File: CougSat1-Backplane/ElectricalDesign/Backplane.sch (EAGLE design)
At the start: 20 parts, among them J1 CougSat Socket, J10 CougSat Socket, J2 CougSat Socket, J3 CougSat Socket, J4 CougSat Socket, J5 Separation Switch, J6 Separation Switch, J7 CougSat Socket, J8 CougSat Socket, J9 CougSat Socket

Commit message: Removed Unused Connectors, Shrunk Outline
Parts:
- removed J1, J2, J3: CougSat Socket, CougsInSpace-Connectors:CIS_CARD-PCIE
- removed J5, J6: Separation Switch, CougsInSpace-Connectors:1X04-PICOLOCK
- removed LOGO1: Text, CougsInSpace-Aesthetics:CIS-LOGO-TEXT
- removed LOGO100, LOGO3: Satellite 16mm, CougsInSpace-Aesthetics:CIS-LOGO-SATELLITE-16MM
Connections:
- net BUS_I2C0_IRQ: no longer J1DATA.BUS_I2C0_IRQ, J2DATA.BUS_I2C0_IRQ, J3DATA.BUS_I2C0_IRQ
- net BUS_I2C0_SCL: no longer J1DATA.BUS_I2C0_SCL, J2DATA.BUS_I2C0_SCL, J3DATA.BUS_I2C0_SCL
- net BUS_I2C0_SDA: no longer J1DATA.BUS_I2C0_SDA, J2DATA.BUS_I2C0_SDA, J3DATA.BUS_I2C0_SDA
- net BUS_I2C1_IRQ: no longer J1DATA.BUS_I2C1_IRQ, J2DATA.BUS_I2C1_IRQ, J3DATA.BUS_I2C1_IRQ
- net BUS_I2C1_SCL: no longer J1DATA.BUS_I2C1_SCL, J2DATA.BUS_I2C1_SCL, J3DATA.BUS_I2C1_SCL
- net BUS_I2C1_SDA: no longer J1DATA.BUS_I2C1_SDA, J2DATA.BUS_I2C1_SDA, J3DATA.BUS_I2C1_SDA
- net BUS_JTAG_EN-0: no longer J1JTAG.BUS_JTAG_EN-0, J2JTAG.BUS_JTAG_EN-0, J3JTAG.BUS_JTAG_EN-0
- net BUS_JTAG_EN-1: no longer J1JTAG.BUS_JTAG_EN-1, J2JTAG.BUS_JTAG_EN-1, J3JTAG.BUS_JTAG_EN-1
- net BUS_JTAG_EN-2: no longer J1JTAG.BUS_JTAG_EN-2, J2JTAG.BUS_JTAG_EN-2, J3JTAG.BUS_JTAG_EN-2
- net BUS_JTAG_EN-3: no longer J1JTAG.BUS_JTAG_EN-3, J2JTAG.BUS_JTAG_EN-3, J3JTAG.BUS_JTAG_EN-3
- net BUS_JTAG_TCK: no longer J1JTAG.BUS_JTAG_TCK, J2JTAG.BUS_JTAG_TCK, J3JTAG.BUS_JTAG_TCK
- net BUS_JTAG_TDI: no longer J1JTAG.BUS_JTAG_TDI, J2JTAG.BUS_JTAG_TDI, J3JTAG.BUS_JTAG_TDI
- net BUS_JTAG_TDO: no longer J1JTAG.BUS_JTAG_TDO, J2JTAG.BUS_JTAG_TDO, J3JTAG.BUS_JTAG_TDO
- net BUS_JTAG_TMS: no longer J1JTAG.BUS_JTAG_TMS, J2JTAG.BUS_JTAG_TMS, J3JTAG.BUS_JTAG_TMS
- net BUS_SPI_MISO: no longer J1DATA.BUS_SPI_MISO, J2DATA.BUS_SPI_MISO, J3DATA.BUS_SPI_MISO
- net BUS_SPI_MOSI: no longer J1DATA.BUS_SPI_MOSI, J2DATA.BUS_SPI_MOSI, J3DATA.BUS_SPI_MOSI
- net BUS_SPI_SCK: no longer J1DATA.BUS_SPI_SCK, J2DATA.BUS_SPI_SCK, J3DATA.BUS_SPI_SCK
- net COM_SPI_CS: no longer J1DATA.COM_SPI_CS, J2DATA.COM_SPI_CS, J3DATA.COM_SPI_CS
- net COM_SPI_MISO: no longer J1DATA.COM_SPI_MISO, J2DATA.COM_SPI_MISO, J3DATA.COM_SPI_MISO
- net COM_SPI_MOSI: no longer J1DATA.COM_SPI_MOSI, J2DATA.COM_SPI_MOSI, J3DATA.COM_SPI_MOSI
- net COM_SPI_SCK: no longer J1DATA.COM_SPI_SCK, J2DATA.COM_SPI_SCK, J3DATA.COM_SPI_SCK
- net CTRL_SYNC: no longer J1DATA.CTRL_SYNC, J2DATA.CTRL_SYNC, J3DATA.CTRL_SYNC
- net GPIO-0: no longer J1GPIO.GPIO-0, J2GPIO.GPIO-0, J3GPIO.GPIO-0
- net GPIO-1: no longer J1GPIO.GPIO-1, J2GPIO.GPIO-1, J3GPIO.GPIO-1
- net GPIO-2: no longer J1GPIO.GPIO-2, J2GPIO.GPIO-2, J3GPIO.GPIO-2
- net GPIO-3: no longer J1GPIO.GPIO-3, J2GPIO.GPIO-3, J3GPIO.GPIO-3
- net GPIO-4: no longer J1GPIO.GPIO-4, J2GPIO.GPIO-4, J3GPIO.GPIO-4
- net GPIO-5: no longer J1GPIO.GPIO-5, J2GPIO.GPIO-5, J3GPIO.GPIO-5
- net GPIO-6: no longer J1GPIO.GPIO-6, J2GPIO.GPIO-6, J3GPIO.GPIO-6
- net GPIO-7: no longer J1GPIO.GPIO-7, J2GPIO.GPIO-7, J3GPIO.GPIO-7
- net PGND: no longer J1POWER.PGND, J2POWER.PGND, J3POWER.PGND, J5.3, J5.4, J6.3, J6.4
- net PR_3.3V-0: no longer J1POWER.PR_3.3V-0, J2POWER.PR_3.3V-0, J3POWER.PR_3.3V-0
- net PR_3.3V-1: no longer J1POWER.PR_3.3V-1, J2POWER.PR_3.3V-1, J3POWER.PR_3.3V-1
- net PR_3.3V-10: no longer J1POWER.PR_3.3V-10, J2POWER.PR_3.3V-10, J3POWER.PR_3.3V-10
- net PR_3.3V-11: no longer J1POWER.PR_3.3V-11, J2POWER.PR_3.3V-11, J3POWER.PR_3.3V-11
- net PR_3.3V-12: no longer J1POWER.PR_3.3V-12, J2POWER.PR_3.3V-12, J3POWER.PR_3.3V-12
- net PR_3.3V-2: no longer J1POWER.PR_3.3V-2, J2POWER.PR_3.3V-2, J3POWER.PR_3.3V-2
- net PR_3.3V-3: no longer J1POWER.PR_3.3V-3, J2POWER.PR_3.3V-3, J3POWER.PR_3.3V-3
- net PR_3.3V-4: no longer J1POWER.PR_3.3V-4, J2POWER.PR_3.3V-4, J3POWER.PR_3.3V-4
- net PR_3.3V-5: no longer J1POWER.PR_3.3V-5, J2POWER.PR_3.3V-5, J3POWER.PR_3.3V-5
- net PR_3.3V-6: no longer J1POWER.PR_3.3V-6, J2POWER.PR_3.3V-6, J3POWER.PR_3.3V-6
- net PR_3.3V-7: no longer J1POWER.PR_3.3V-7, J2POWER.PR_3.3V-7, J3POWER.PR_3.3V-7
- net PR_3.3V-8: no longer J1POWER.PR_3.3V-8, J2POWER.PR_3.3V-8, J3POWER.PR_3.3V-8
- net PR_3.3V-9: no longer J1POWER.PR_3.3V-9, J2POWER.PR_3.3V-9, J3POWER.PR_3.3V-9
- net PR_BATT-0: no longer J1POWER.PR_BATT-0, J2POWER.PR_BATT-0, J3POWER.PR_BATT-0
- net PR_BATT-1: no longer J1POWER.PR_BATT-1, J2POWER.PR_BATT-1, J3POWER.PR_BATT-1
- net PR_BATT-2: no longer J1POWER.PR_BATT-2, J2POWER.PR_BATT-2, J3POWER.PR_BATT-2
- net PR_BATT-3: no longer J1POWER.PR_BATT-3, J2POWER.PR_BATT-3, J3POWER.PR_BATT-3
- net PR_BATT-4: no longer J1POWER.PR_BATT-4, J2POWER.PR_BATT-4, J3POWER.PR_BATT-4
- net PR_BATT-5: no longer J1POWER.PR_BATT-5, J2POWER.PR_BATT-5, J3POWER.PR_BATT-5
- net PR_BATT-6: no longer J1POWER.PR_BATT-6, J2POWER.PR_BATT-6, J3POWER.PR_BATT-6
- net PWR_CTRL_SW: no longer J1POWER.PWR_CTRL_SW, J2POWER.PWR_CTRL_SW, J3POWER.PWR_CTRL_SW, J5.1, J5.2, J6.1, J6.2
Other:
- moved on the sheet: LOGO2

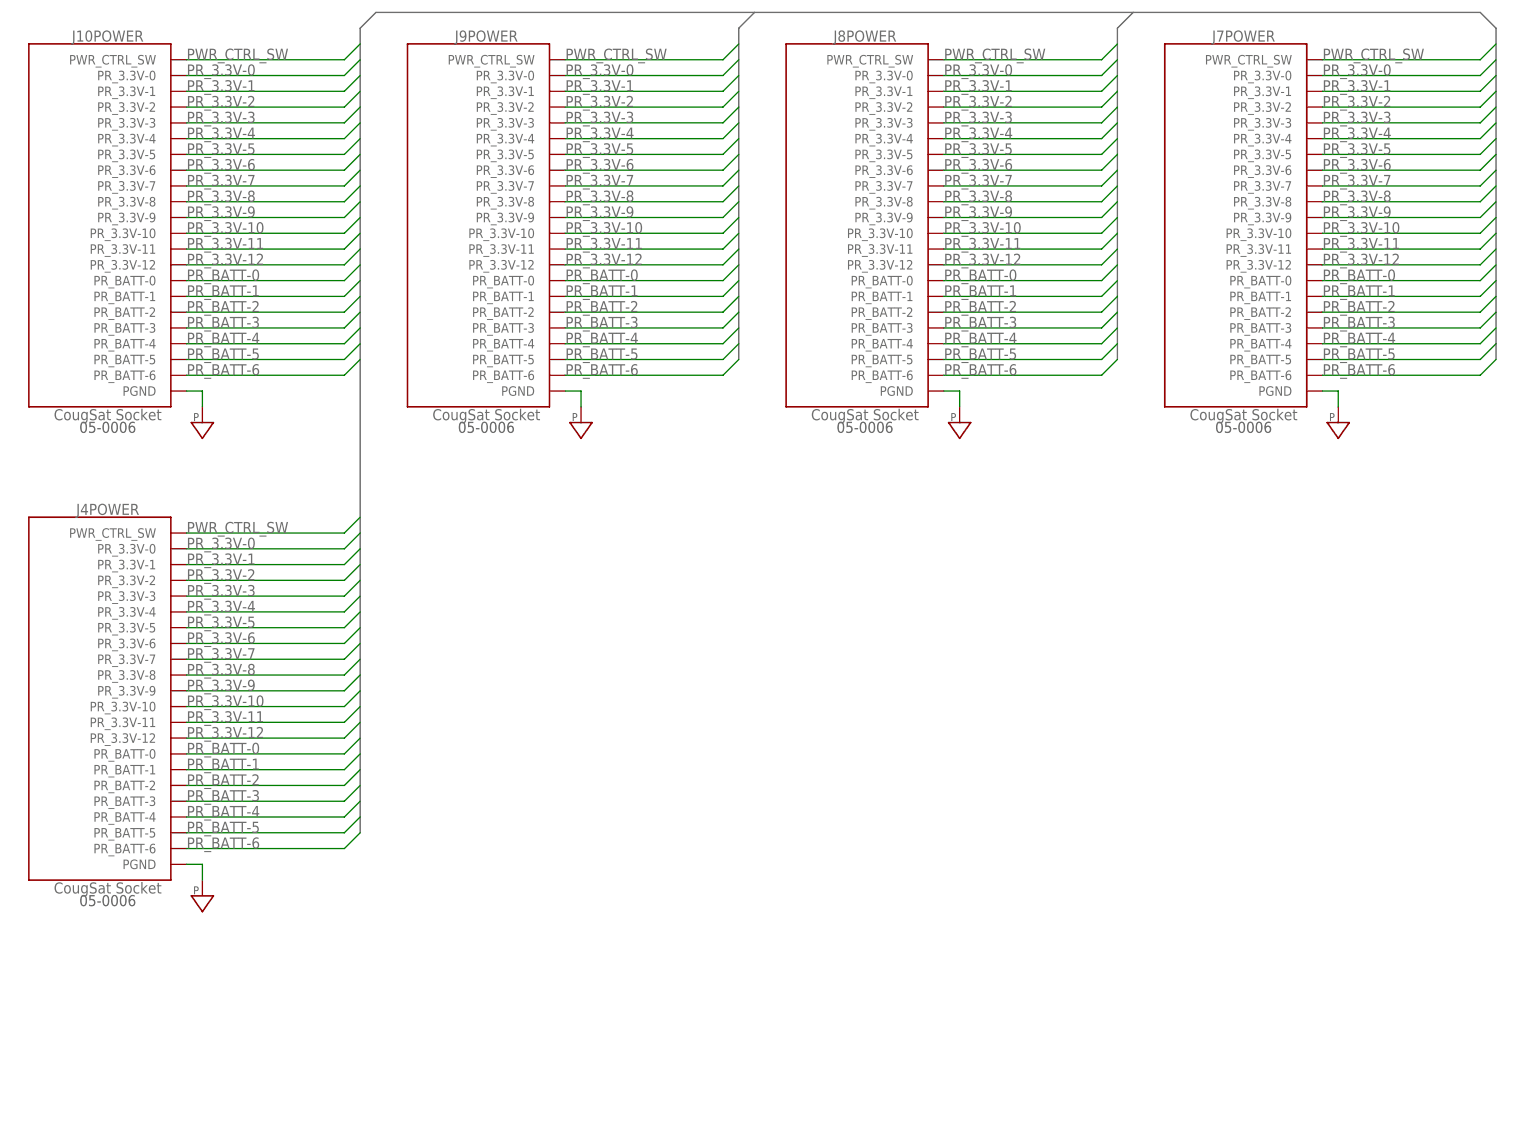
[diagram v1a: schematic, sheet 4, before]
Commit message: Made board and schematic pretty again
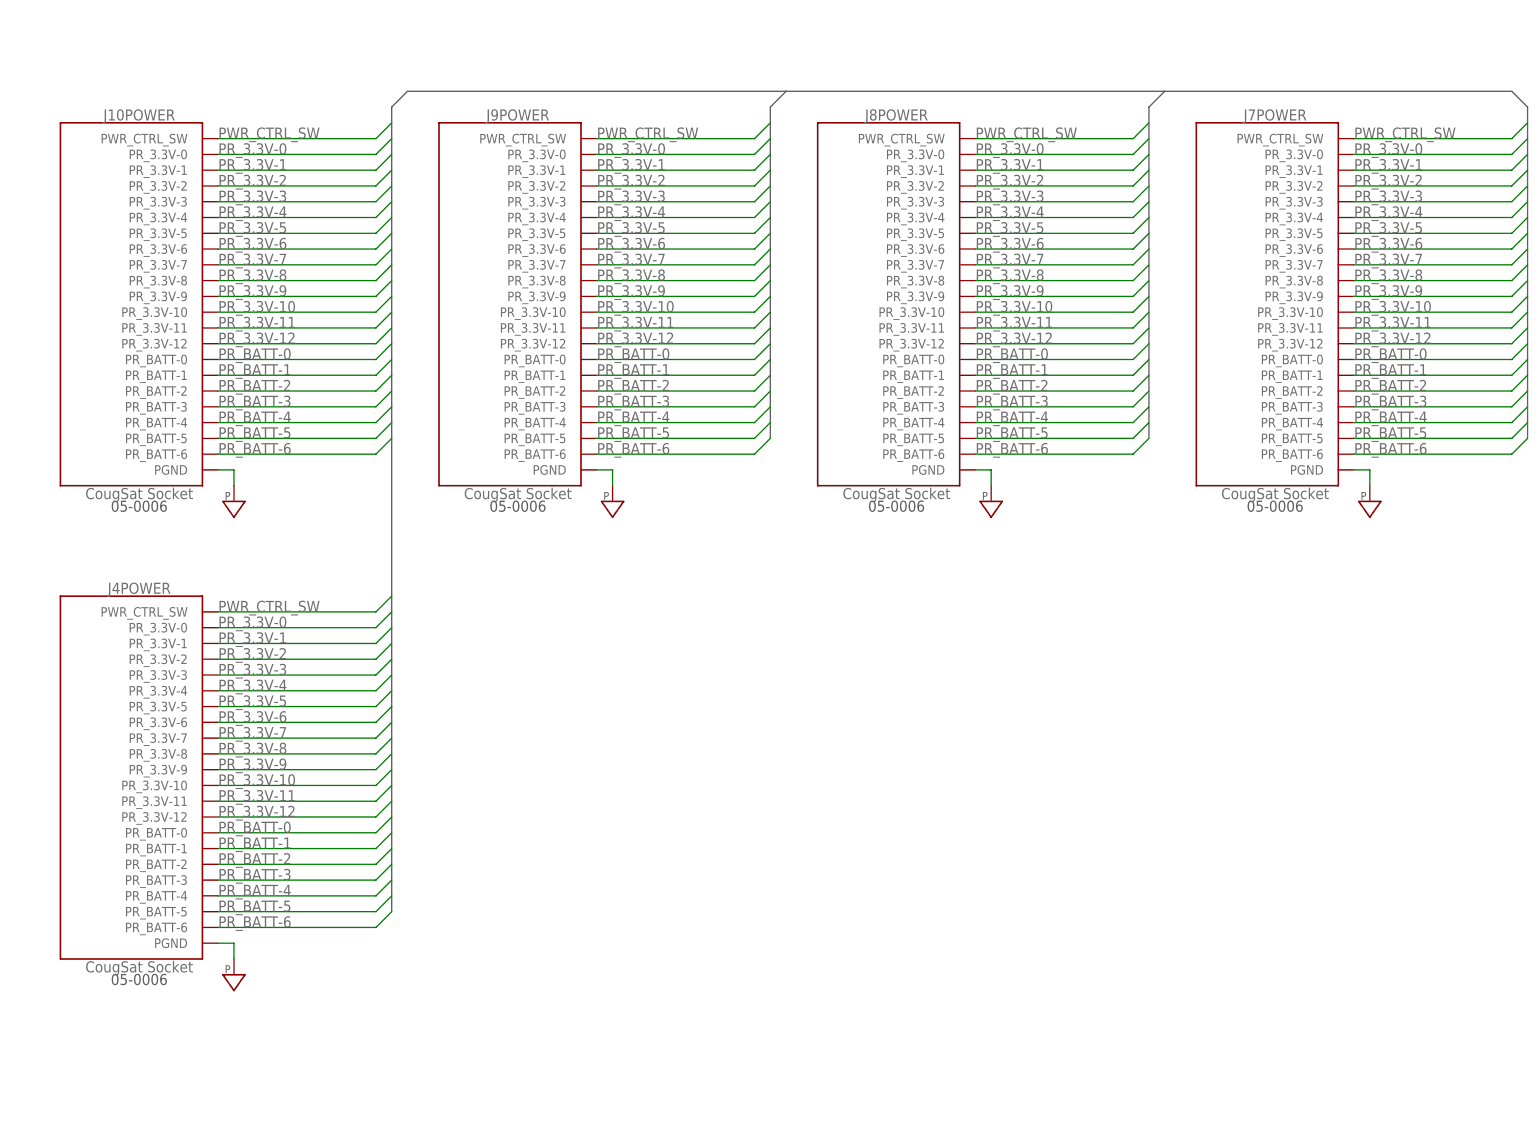
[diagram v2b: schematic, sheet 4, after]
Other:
- note added: "<3A4>"
- note added: "<3B4>"
- note added: "<3C4>"
- note removed: "<3A6>"
- note removed: "<3B6>"
- note removed: "<3C6>"
- note removed: "Connector: Deployment Switch"
- note removed: "Page 4"
- note removed: "Slot 5"
- note removed: "Slot 6"
- note removed: "Slot 7"
- moved on the sheet: J10POWER, J4DATA, J4GPIO, J4JTAG, J4POWER, J7POWER, J8POWER, J9POWER

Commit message: Fixed polygon rank reference designators
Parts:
- renumbered J10 to J0, J7 to J3, J8 to J2, J9 to J1
